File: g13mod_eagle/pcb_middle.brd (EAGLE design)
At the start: 134.2 x 33.2 mm, 71 parts

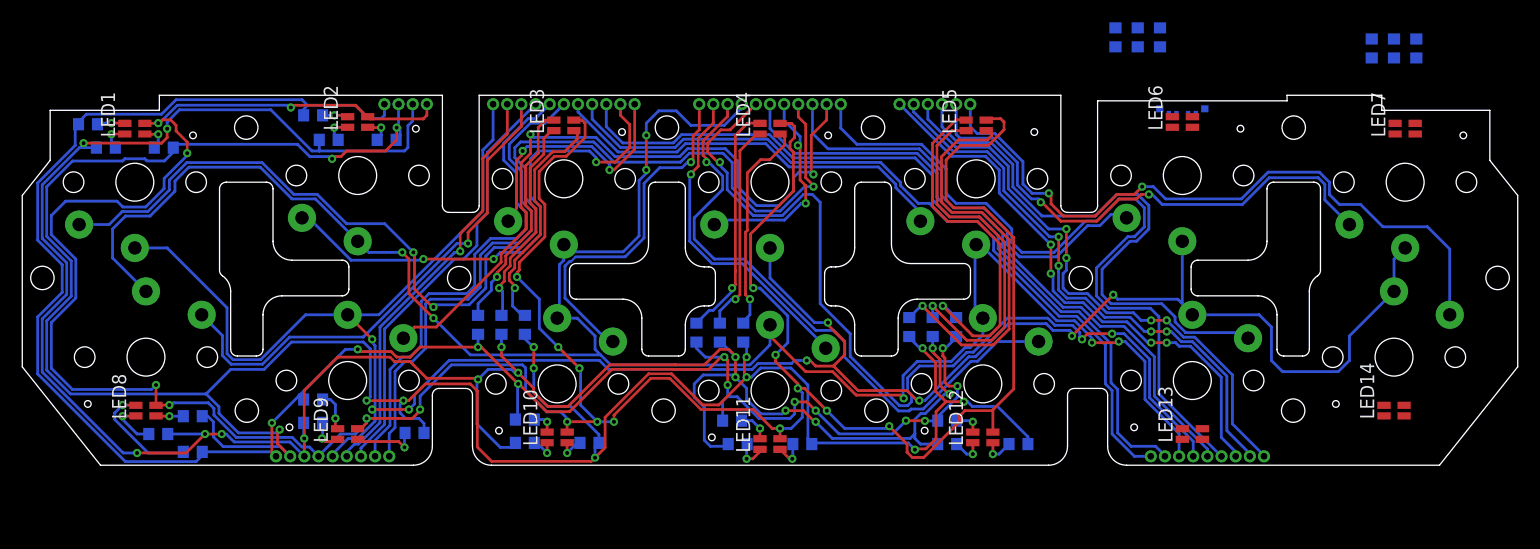
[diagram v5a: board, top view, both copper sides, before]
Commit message: wiring middle pcb
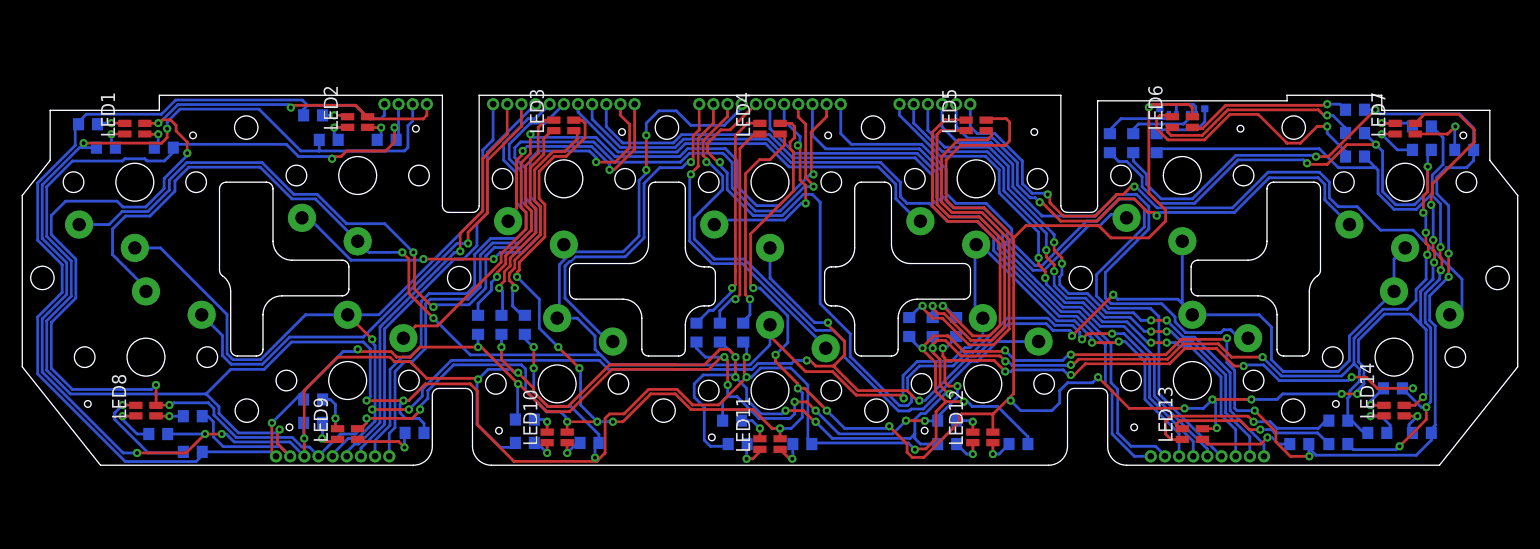
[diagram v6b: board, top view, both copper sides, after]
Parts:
- added R37, R38, R39, R40, R41, R42, R43, R44, R45: (no value), rcl:R0603
- moved R18 22.5 mm to (52.5, 6.50), turned to 0 degrees
- moved R16 21.3 mm to (52.5, 4.40), turned to 0 degrees
- moved R17 20.5 mm to (52.5, 2.30), turned to 0 degrees
- moved R21 12.3 mm to (62.3, 2.90), turned to 0 degrees
- moved R19 9.44 mm to (58.5, 2.90), turned to 0 degrees
- moved R20 7.02 mm to (58.5, 5.00), turned to 0 degrees
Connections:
- new net N$37: LED13.1, R37.2
- new net N$38: LED13.2, R38.2
- new net N$39: LED13.4, R39.2
- new net N$40: LED14.1, R40.2
- new net N$41: LED14.2, R41.2
- new net N$42: LED14.4, R42.2
- new net N$43: D1.2, R43.2
- new net N$44: D1.6, R44.2
- new net N$45: D1.4, R45.2
- net B: now also R38.1, R41.1, R44.1
- net G: now also R37.1, R40.1, R43.1
- net R: now also R39.1, R42.1, R45.1
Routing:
- net R: track 231.6 -> 358.7 mm, vias 13 -> 22
- net V: track 279.6 -> 403.6 mm, vias 19 -> 32
- net B: track 181.8 -> 298.2 mm, vias 12 -> 21
- net G: track 209.2 -> 325.0 mm, vias 15 -> 24
- net N$17: track 0.00 -> 24.2 mm, vias 0 -> 1
- net N$16: track 0.00 -> 19.0 mm, vias 0 -> 1
- net N$37: track 0.00 -> 18.4 mm, vias 0 -> 1
- net N$38: track 0.00 -> 15.4 mm, vias 0 -> 1
- net N$18: track 0.00 -> 14.9 mm, vias 0 -> 1
- net N$39: track 0.00 -> 9.02 mm, vias 0 -> 1
- net N$43: track 0.00 -> 6.18 mm
- net N$45: track 0.00 -> 6.06 mm
- net N$21: track 0.00 -> 6.00 mm, vias 0 -> 1
- net N$44: track 0.00 -> 5.93 mm
- net N$20: track 0.00 -> 4.59 mm, vias 0 -> 1
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
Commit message: Edit width
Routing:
- net V: track 403.6 -> 409.6 mm, vias 32 -> 30
- net B: track 298.2 -> 300.6 mm
- net R: track 358.7 -> 361.0 mm
- net G: track 325.0 -> 326.6 mm
- net CN7_12: track 18.9 -> 19.6 mm
- net CN7_11: track 104.4 -> 105.0 mm

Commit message: Fix bug
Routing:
- net V: track 409.6 -> 404.0 mm
- net CN6_18: track 205.8 -> 204.7 mm
- net CN7_15: track 186.3 -> 185.5 mm
- net G: track 326.6 -> 326.0 mm
- net N$20: track 4.59 -> 4.08 mm
- net N$39: track 9.02 -> 8.52 mm
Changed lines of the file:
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@@
 <wire x1="-50.9" y1="-24.47255" x2="-50.9" y2="-24.2" width="0.254" layer="16"/>
 <contactref element="R26" pad="1"/>
-<wire x1="-41.85" y1="-19.5" x2="-41.7" y2="-19.5" width="0.254" layer="16"/>
 <wire x1="-43.05" y1="-19.15" x2="-44.7" y2="-20.8" width="0.254" layer="16"/>
 <wire x1="-44.7" y1="-21.2" x2="-44.7" y2="-20.8" width="0.254" layer="16"/>
@@
 <wire x1="-34.6" y1="6.995" x2="-34.605" y2="7" width="0.254" layer="16"/>
 <wire x1="-37.2" y1="6.9" x2="-36" y2="5.7" width="0.254" layer="16"/>
-<wire x1="-41.7" y1="6.15" x2="-41.85" y2="6" width="0.254" layer="16"/>
 <wire x1="-41.85" y1="6" x2="-41.875" y2="6.025" width="0.254" layer="16"/>
 <wire x1="-41.875" y1="6.025" x2="-41.875" y2="6.525" width="0.254" layer="16"/>
@@
 <via x="-33.7" y="4.9" extent="1-16" drill="0.35"/>
 <contactref element="R27" pad="1"/>
-<wire x1="-43.06" y1="-24.56" x2="-43.06" y2="-24.6" width="0.254" layer="1"/>
 <via x="-32.9" y="-19.6" extent="1-16" drill="0.35"/>
 <wire x1="-32.9" y1="-19.6" x2="-33.2" y2="-19.9" width="0.254" layer="16"/>
@@
 <wire x1="-35.873" y1="-19.273" x2="-36.2" y2="-19.6" width="0.254" layer="16"/>
 <wire x1="-35.873" y1="-14.9603875" x2="-35.873" y2="-19.273" width="0.254" layer="16"/>
-<wire x1="-33.435" y1="4.9" x2="-33.7" y2="4.9" width="0.254" layer="16"/>
 <contactref element="R30" pad="1"/>
 <wire x1="-21.25" y1="-14.8" x2="-22" y2="-14.05" width="0.254" layer="16"/>
@@
 <wire x1="-56.8" y1="-24.3" x2="-52.4" y2="-24.3" width="0.254" layer="1"/>
 <wire x1="-52.4" y1="-24.3" x2="-50.7" y2="-22.6" width="0.254" layer="1"/>
-<wire x1="-60.75" y1="2.8" x2="-60.45" y2="3.1" width="0.254" layer="16"/>
 <via x="-61.6" y="3.5" extent="1-16" drill="0.35"/>
 <wire x1="-54.6" y1="3.5" x2="-61.6" y2="3.5" width="0.254" layer="1"/>
@@
 <wire x1="53.3" y1="-22.5" x2="53.65" y2="-22.5" width="0.254" layer="16"/>
 <wire x1="52.2" y1="-21.4" x2="53.3" y2="-22.5" width="0.254" layer="16"/>
-<wire x1="51.85" y1="-21.4" x2="52" y2="-21.25" width="0.254" layer="16"/>
 <wire x1="52.4064" y1="-16.2936" x2="52.4064" y2="-14" width="0.254" layer="16"/>
 <wire x1="52.4064" y1="-14" x2="54.4064" y2="-12" width="0.254" layer="16"/>
@@
 <via x="-22.7" y="-8.5" extent="1-16" drill="0.35"/>
 <via x="-19" y="-14.8" extent="1-16" drill="0.35"/>
-<wire x1="-18.2" y1="-21.2" x2="-18.7936" y2="-20.6064" width="0.254" layer="16"/>
-<wire x1="-18.7936" y1="-20.6064" x2="-20.03495" y2="-20.6064" width="0.254" layer="16"/>
 <wire x1="-55.1" y1="-20" x2="-55.1" y2="-20.025" width="0.254" layer="1"/>
 <via x="-55.1" y="-18.3" extent="1-16" drill="0.35"/>
 <via x="-54.4" y="0.5" extent="1-16" drill="0.35"/>
-<wire x1="-37" y1="-22.125" x2="-36.725" y2="-22.125" width="0.254" layer="1"/>
 <wire x1="-64.5" y1="-12.8" x2="-64.5" y2="-13" width="0.254" layer="16"/>
 <via x="0.9" y="-22.1" extent="1-16" drill="0.35"/>
@@
 <via x="-1.5" y="-9.5" extent="1-16" drill="0.35"/>
 <via x="-15.5" y="-21.5" extent="1-16" drill="0.35"/>
-<wire x1="-17" y1="-16.8" x2="-17.1" y2="-16.7" width="0.254" layer="16"/>
-<wire x1="-17" y1="-16.8" x2="-17" y2="-18" width="0.254" layer="16"/>
 <via x="-17.1" y="-16.7" extent="1-16" drill="0.35"/>
 <via x="-14.1" y="-21.5" extent="1-16" drill="0.35"/>
-<wire x1="19.4" y1="5.575" x2="19.525" y2="5.7" width="0.254" layer="1"/>
 <wire x1="21.7625" y1="-19.0625" x2="21.8686" y2="-18.9564" width="0.254" layer="1"/>
 <wire x1="21.4125" y1="-19.4125" x2="20" y2="-20.825" width="0.254" layer="1"/>
 <via x="6.1" y="-21.5" extent="1-16" drill="0.35"/>
 <via x="10.7" y="-21.9" extent="1-16" drill="0.35"/>
-<wire x1="36.47" y1="6" x2="36.5" y2="6.03" width="0.2032" layer="16"/>
 <via x="34" y="6.72125" extent="1-16" drill="0.35"/>
 <wire x1="36.5" y1="6.97245" x2="38" y2="6.97245" width="0.254" layer="16"/>
@@
 <via x="59.8" y="-7.4" extent="1-16" drill="0.35"/>
 <wire x1="37.9" y1="6" x2="37.9" y2="5.875" width="0.254" layer="1"/>
-<wire x1="37.7875" y1="6.7875" x2="37.60255" y2="6.97245" width="0.254" layer="1"/>
-<wire x1="37" y1="6.97245" x2="37.60255" y2="6.97245" width="0.254" layer="1"/>
-<wire x1="34.9975" y1="6.8025" x2="34.82755" y2="6.97245" width="0.254" layer="16"/>
 <wire x1="34.2512" y1="6.97245" x2="34" y2="6.72125" width="0.254" layer="16"/>
 <wire x1="34.2512" y1="6.97245" x2="34.82755" y2="6.97245" width="0.254" layer="16"/>
@@
 <wire x1="21.8686" y1="-18.9564" x2="22" y2="-18.825" width="0.508" layer="1"/>
 <wire x1="22" y1="-18.825" x2="22" y2="-5.3956" width="0.508" layer="1"/>
-<wire x1="22" y1="-5.3956" x2="22" y2="-4.8686" width="0.508" layer="1"/>
 <wire x1="19.4" y1="5.575" x2="20.425" y2="5.575" width="0.508" layer="1"/>
 <wire x1="20.425" y1="5.575" x2="21" y2="5" width="0.508" layer="1"/>
@@
 <via x="-32.4" y="-20.4" extent="1-16" drill="0.35"/>
 <via x="-35.7" y="-20.4" extent="1-16" drill="0.35"/>
-<wire x1="-37.9" y1="-11.9" x2="-36.8" y2="-11.9" width="0.254" layer="16"/>
 <via x="-35.7" y="-14.1" extent="1-16" drill="0.35"/>
 <wire x1="-35.7" y1="-14.1" x2="-37.9" y2="-11.9" width="0.254" layer="1"/>
@@
 <wire x1="-30.9" y1="-14.9" x2="-30.9" y2="-10.9" width="0.254" layer="16"/>
 <wire x1="-21.4064" y1="-2.5936" x2="-22.3128" y2="-1.6872" width="0.254" layer="16"/>
-<wire x1="-21.4064" y1="-4.3316625" x2="-21.4064" y2="-4.3064" width="0.254" layer="16"/>
 <wire x1="-21.4064" y1="-4.3064" x2="-21.4064" y2="-2.5936" width="0.254" layer="16"/>
 <wire x1="-34.17" y1="-24.6" x2="-34.17" y2="-22.5400125" width="0.254" layer="16"/>
@@
 <wire x1="-14.8" y1="-14" x2="-18.4" y2="-10.4" width="0.254" layer="16"/>
 <wire x1="-18.4" y1="-10.4" x2="-18.4" y2="-7.5254" width="0.254" layer="16"/>
-<wire x1="-18.024" y1="-7.124" x2="-17.9986" y2="-7.124" width="0.2032" layer="16"/>
 <wire x1="-17.8687375" y1="-7.124" x2="-17.4447375" y2="-6.7" width="0.2032" layer="16"/>
 <wire x1="-9.9" y1="1.3" x2="-7.9" y2="1.3" width="0.254" layer="16"/>
@@
 <contactref element="JP3" pad="10"/>
 <contactref element="G11" pad="CHOC2"/>
-<wire x1="-5.08" y1="7" x2="-5.08" y2="6.92" width="0.254" layer="1"/>
 <via x="-7.1" y="0.7" extent="1-16" drill="0.35"/>
 <wire x1="5" y1="-14.1" x2="5" y2="-14.9" width="0.254" layer="16"/>
@@
 <via x="28.9" y="-14.4" extent="1-16" drill="0.35"/>
 <wire x1="28.9" y1="-14" x2="28.9" y2="-14.4" width="0.254" layer="16"/>
-<wire x1="19" y1="-12.2" x2="19.1" y2="-12.2" width="0.254" layer="16"/>
 <via x="12" y="-19.4" extent="1-16" drill="0.35"/>
 <wire x1="36.71" y1="-24.6" x2="36.71" y2="-22.559475" width="0.254" layer="16"/>
@@
 <wire x1="18.5" y1="-6.5" x2="18.4" y2="-6.6" width="0.254" layer="16"/>
 <wire x1="18.4" y1="-6.6" x2="18.4" y2="-11.5" width="0.254" layer="16"/>
-<wire x1="19" y1="-12.2" x2="18.5" y2="-11.7" width="0.254" layer="16"/>
 <wire x1="-19.1" y1="-12.2" x2="-18.9" y2="-12" width="0.254" layer="16"/>
 <wire x1="-18.9" y1="-12" x2="-18.9" y2="-7.4" width="0.254" layer="16"/>
@@
 <contactref element="R16" pad="2"/>
 <contactref element="LED6" pad="1"/>
-<wire x1="51.65" y1="4.4" x2="51.6" y2="4.4" width="0.2032" layer="16"/>
 <via x="50" y="6" extent="1-16" drill="0.35"/>
 <wire x1="51.65" y1="4.4" x2="51.65" y2="4.85" width="0.254" layer="16"/>
@@
 <contactref element="R20" pad="2"/>
 <contactref element="LED7" pad="2"/>
-<wire x1="57.65" y1="5" x2="57.6" y2="5" width="0.2032" layer="16"/>
-<wire x1="57.6" y1="5" x2="57.3" y2="5.3" width="0.2032" layer="16"/>
 <via x="54.9" y="5.3" extent="1-16" drill="0.35"/>
-<wire x1="56.075" y1="5.3" x2="56.1" y2="5.275" width="0.2032" layer="1"/>
 <wire x1="56.1" y1="5.275" x2="54.925" y2="5.275" width="0.254" layer="1"/>
 <wire x1="54.925" y1="5.275" x2="54.9" y2="5.3" width="0.254" layer="1"/>
@@
 <contactref element="R27" pad="2"/>
 <contactref element="LED9" pad="4"/>
-<wire x1="-33" y1="-22.75" x2="-32.75" y2="-22.5" width="0.254" layer="16"/>
 <wire x1="-32.8" y1="-23.8" x2="-33.325" y2="-23.275" width="0.254" layer="1"/>
 <wire x1="-33.325" y1="-23.275" x2="-36.8" y2="-23.275" width="0.254" layer="1"/>
@@
 <contactref element="LED13" pad="4"/>
 <via x="44.6387875" y="-22.9088" extent="1-16" drill="0.35"/>
-<wire x1="38.8" y1="-23.075" x2="39.3" y2="-23.075" width="0.2032" layer="1"/>
 <wire x1="46.65" y1="-23.5" x2="45.65" y2="-23.5" width="0.254" layer="16"/>
 <wire x1="45.65" y1="-23.5" x2="45.0588" y2="-22.9088" width="0.254" layer="16"/>
